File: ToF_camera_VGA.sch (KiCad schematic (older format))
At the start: 70 parts, among them J1 54548-2271_connector_RPi_zero, J10 Conn_01x01, J11 Conn_01x01, J12 Conn_01x01, J13 Conn_01x01, J14 Conn_01x01, J15 Conn_01x01, J16 Conn_01x01, J17 Conn_01x01, J18 Conn_01x01, J2 Conn_01x01, J3 Conn_01x04, J4 Conn_01x01, J5 Conn_01x04, J6 Conn_01x04, J7 Conn_01x02, J9 Conn_01x03, SW1 SW_Push, U1 LP5907MFX-1.8, U2 MLX75027, U3 LP5907MFX-1.2, U4 LP5907MFX-2.8, U5 PCA9306, U6 TPS82130, Y1 DSC6011JI1A-008.0000_clock_so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

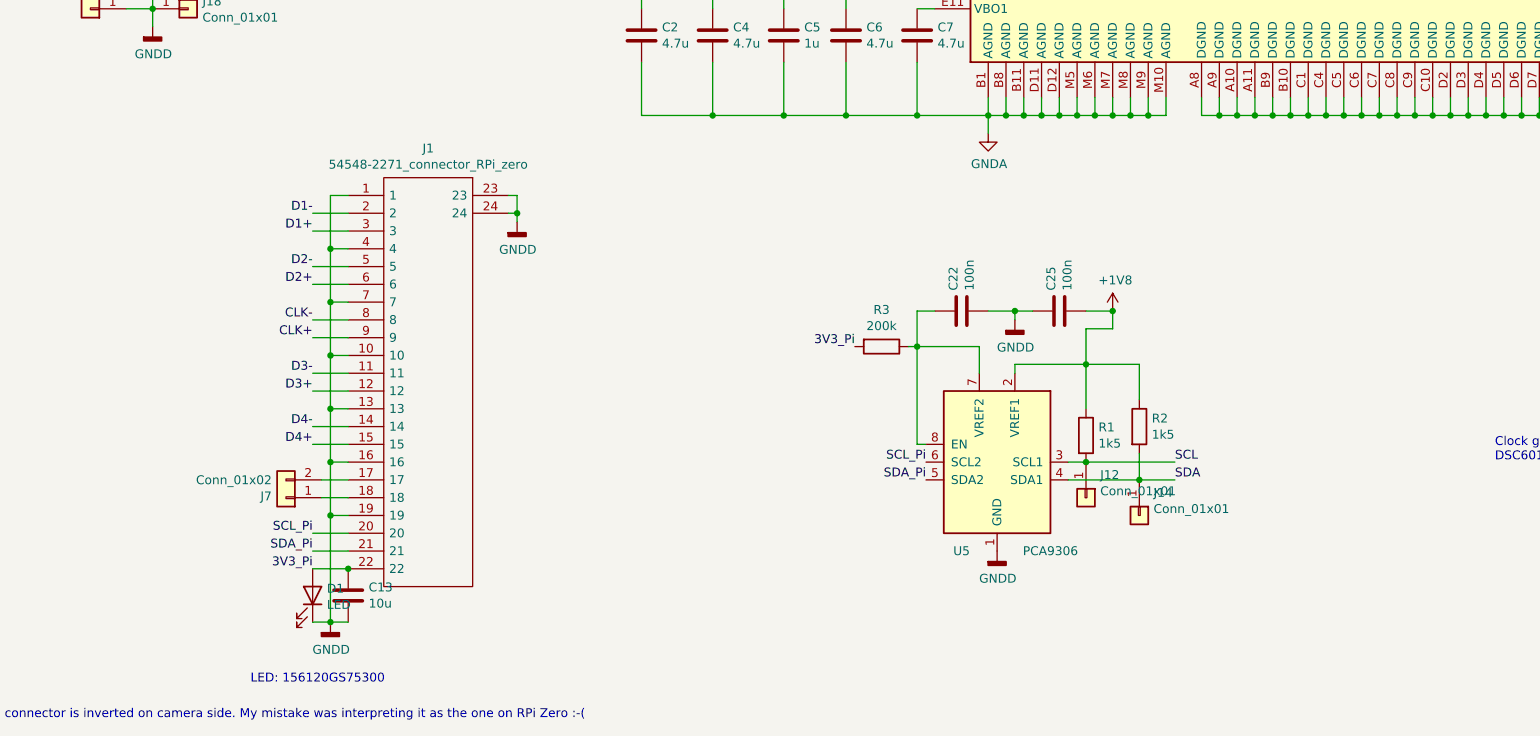
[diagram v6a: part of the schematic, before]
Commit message: Flat cable connector fixed. The right part is Molex 5034802200
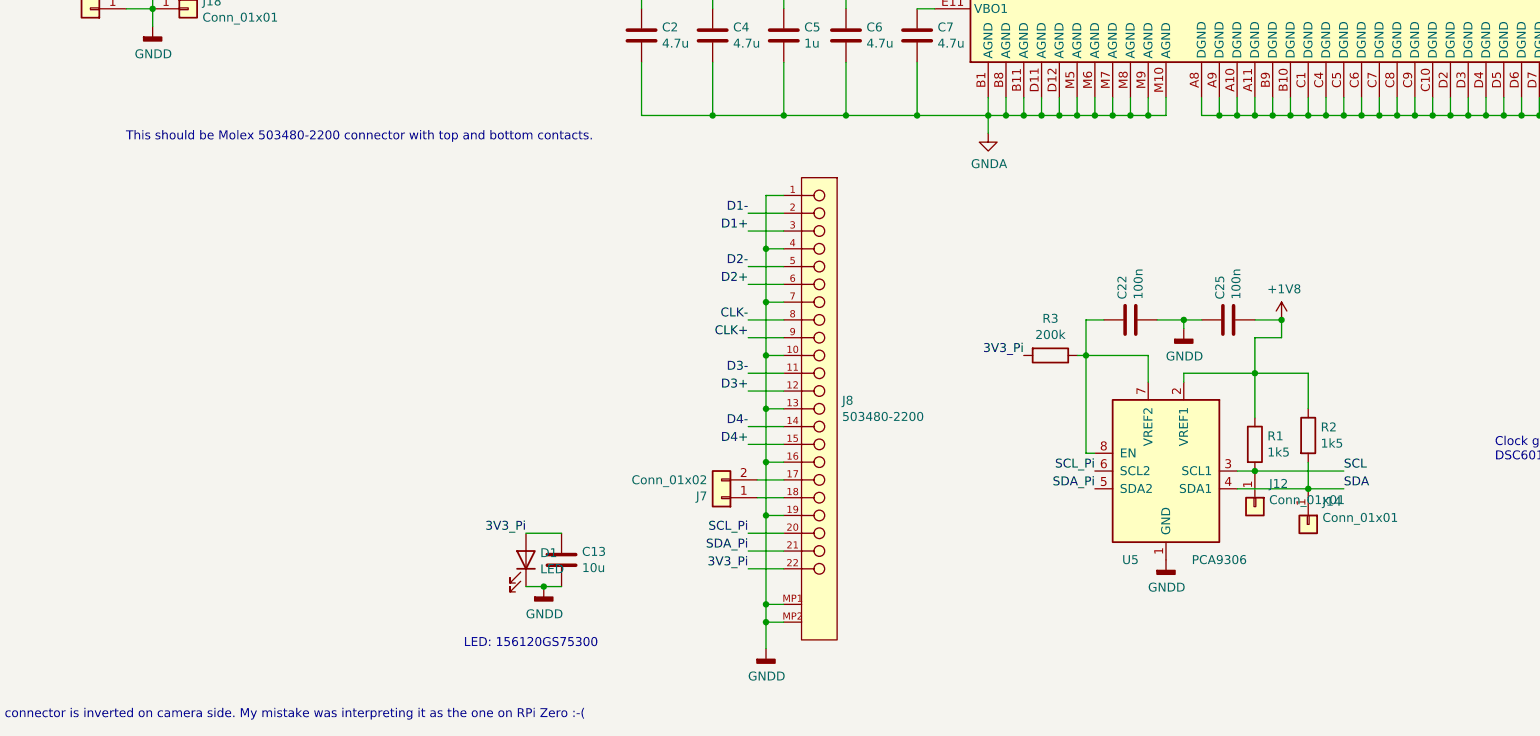
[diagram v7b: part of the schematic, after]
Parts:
- removed J1: 54548-2271_connector_RPi_zero, myFootprints:545482271_RPi_Zero_connector, symbol myParts:54548-2271_connector_RPi_zero
- added J8: 503480-2200, myFootprints:Molex-503480-2200, symbol myParts:503480-2200
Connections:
- net 3V3_Pi: now also J8.22
- net CLK+: now also J8.9
- net CLK-: now also J8.8
- net D1+: now also J8.3
- net D1-: now also J8.2
- net D2+: now also J8.6
- net D2-: now also J8.5
- net D3+: now also J8.12
- net D3-: now also J8.11
- net D4+: now also J8.15
- net D4-: now also J8.14
- net GNDD: now also J8.1, J8.10, J8.13, J8.16, J8.19, J8.4, J8.7, J8.MP1, J8.MP2
- net SCL_Pi: now also J8.20
- net SDA_Pi: now also J8.21
- net at J7.1 (Pin_1): now also J8.18
- net at J7.2 (Pin_2): now also J8.17
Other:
- note added: "This should be Molex 503480-2200 connector with top and bottom contacts."
- moved on the sheet: C13, C22, C25, D1, J12, J14, J7, R1, R2, R3, U5
